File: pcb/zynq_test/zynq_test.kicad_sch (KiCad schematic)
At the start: 0 parts

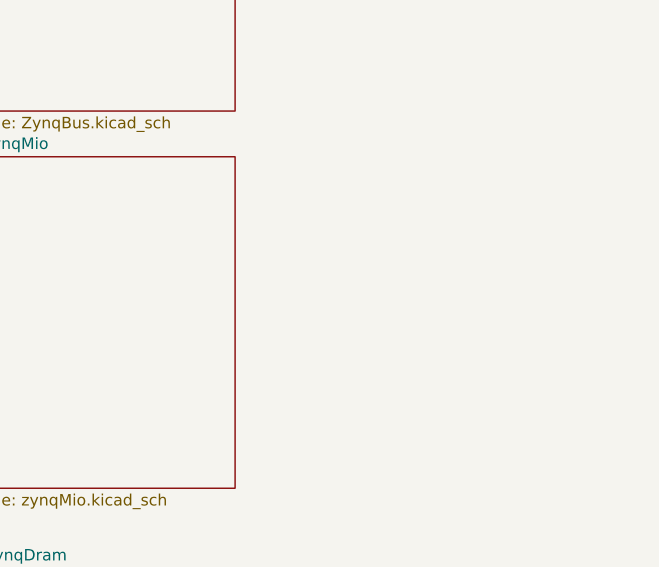
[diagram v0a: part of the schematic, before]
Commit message: Changed MIO signals to Buses
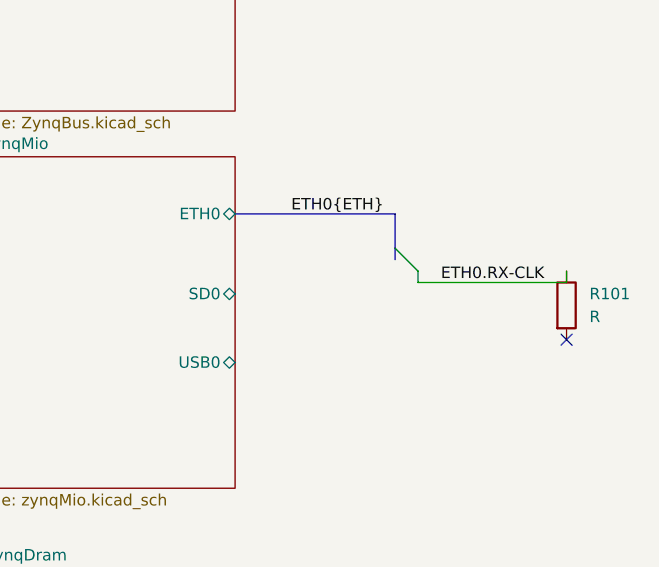
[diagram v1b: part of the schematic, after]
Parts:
- added R101: R, Capacitor_SMD:C_0805_2012Metric, symbol Device:R
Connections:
- new net ETH0.RX-CLK: R101.1
- no-connect marks 0 -> 1
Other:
- sheet zynqMio ports: added ETH0, SD0, USB0; removed none
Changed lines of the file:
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@@
 	(generator_version "9.0")
 	(paper "A4")
+	(no_connect
+		(at 170.18 83.82)
+	)
+	(bus_entry
+		(at 151.13 73.66)
+		(size 2.54 2.54)
+		(stroke
+			(width 0)
+			(type default)
+		)
+	)
+	(bus
+		(pts
+			(xy 151.13 69.85) (xy 151.13 73.66)
+		)
+		(stroke
+			(width 0)
+			(type default)
+		)
+	)
+	(wire
+		(pts
+			(xy 153.67 77.47) (xy 170.18 77.47)
+		)
+		(stroke
+			(width 0)
+			(type default)
+		)
+	)
+	(wire
+		(pts
+			(xy 170.18 77.47) (xy 170.18 76.2)
+		)
+		(stroke
+			(width 0)
+			(type default)
+		)
+	)
+	(wire
+		(pts
+			(xy 153.67 76.2) (xy 153.67 77.47)
+		)
+		(stroke
+			(width 0)
+			(type default)
+		)
+	)
+	(bus
+		(pts
+			(xy 133.35 69.85) (xy 151.13 69.85)
+		)
+		(stroke
+			(width 0)
+			(type default)
+		)
+	)
+	(bus
+		(pts
+			(xy 151.13 73.66) (xy 151.13 74.93)
+		)
+		(stroke
+			(width 0)
+			(type default)
+		)
+	)
+	(label "ETH0{ETH}"
+		(at 149.86 69.85 180)
+		(effects
+			(font
+				(size 1.27 1.27)
+			)
+			(justify right bottom)
+		)
+	)
+	(label "ETH0.RX-CLK"
+		(at 156.21 77.47 0)
+		(effects
+			(font
+				(size 1.27 1.27)
+			)
+			(justify left bottom)
+		)
+	)
+	(symbol
+		(lib_id "Device:R")
+		(at 170.18 80.01 0)
+		(unit 1)
+		(exclude_from_sim no)
+		(in_bom yes)
+		(on_board yes)
+		(dnp no)
+		(fields_autoplaced yes)
+		(property "Reference" "R101"
+			(at 172.72 78.7399 0)
+			(effects
+				(font
+					(size 1.27 1.27)
+				)
+				(justify left)
+			)
+		)
+		(property "Value" "R"
+			(at 172.72 81.2799 0)
+			(effects
+				(font
+					(size 1.27 1.27)
+				)
+				(justify left)
+			)
+		)
+		(property "Footprint" "Capacitor_SMD:C_0805_2012Metric"
+			(at 168.402 80.01 90)
+			(effects
+				(font
+					(size 1.27 1.27)
+				)
+				(hide yes)
+			)
+		)
+		(property "Datasheet" "~"
+			(at 170.18 80.01 0)
+			(effects
+				(font
+					(size 1.27 1.27)
+				)
+				(hide yes)
+			)
+		)
+		(property "Description" "Resistor"
+			(at 170.18 80.01 0)
+			(effects
+				(font
+					(size 1.27 1.27)
+				)
+				(hide yes)
+			)
+		)
+		(pin "1"
+		)
+		(pin "2"
+		)
+		(instances
+			(project ""
+				(path "/0637578d-4ce5-4d31-b973-2de977269ea5"
+					(reference "R101")
+					(unit 1)
+				)
+			)
+		)
+	)
 	(sheet
 		(at 105.41 148.59)
@@
 			)
 		)
+		(pin "ETH0" bidirectional
+			(at 133.35 69.85 0)
+			(effects
+				(font
+					(size 1.27 1.27)
+				)
+				(justify right)
+			)
+		)
+		(pin "SD0" bidirectional
+			(at 133.35 78.74 0)
+			(effects
+				(font
+					(size 1.27 1.27)
+				)
+				(justify right)
+			)
+		)
+		(pin "USB0" bidirectional
+			(at 133.35 86.36 0)
+			(effects
+				(font
+					(size 1.27 1.27)
+				)
+				(justify right)
+			)
+		)

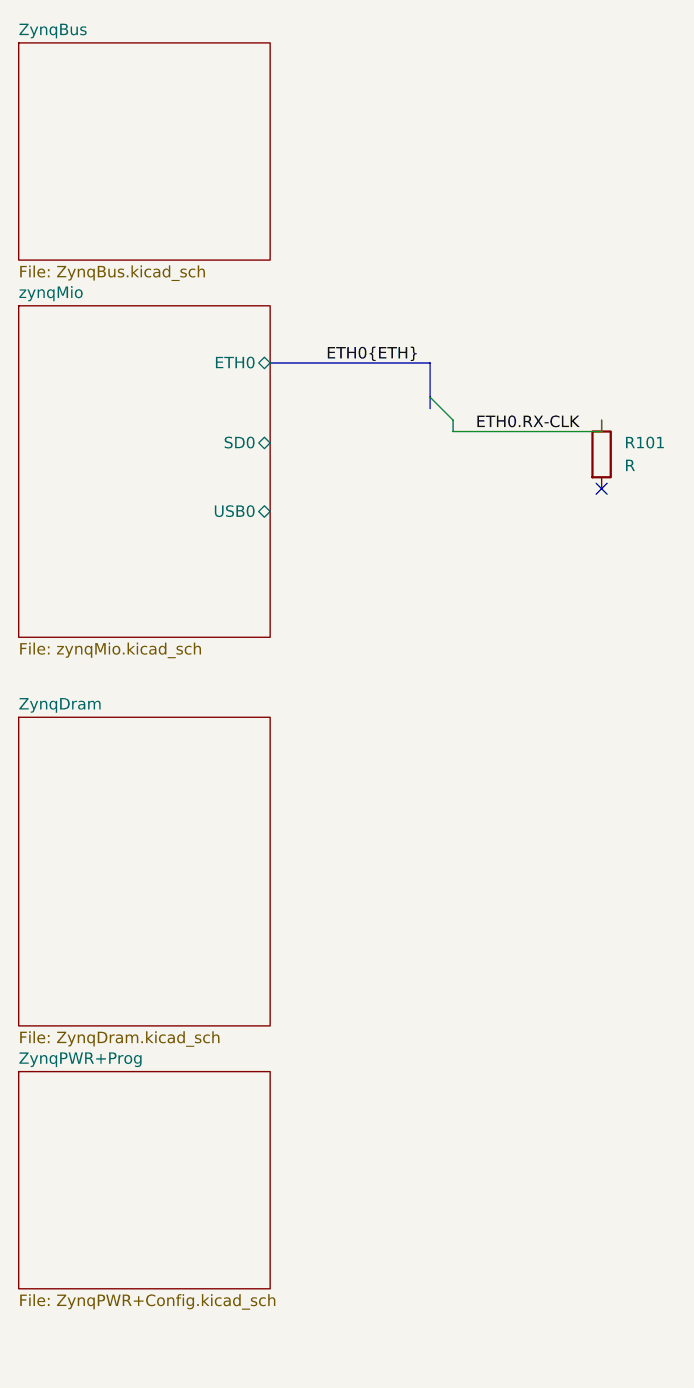
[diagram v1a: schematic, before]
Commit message: Finished PS, started on PWR
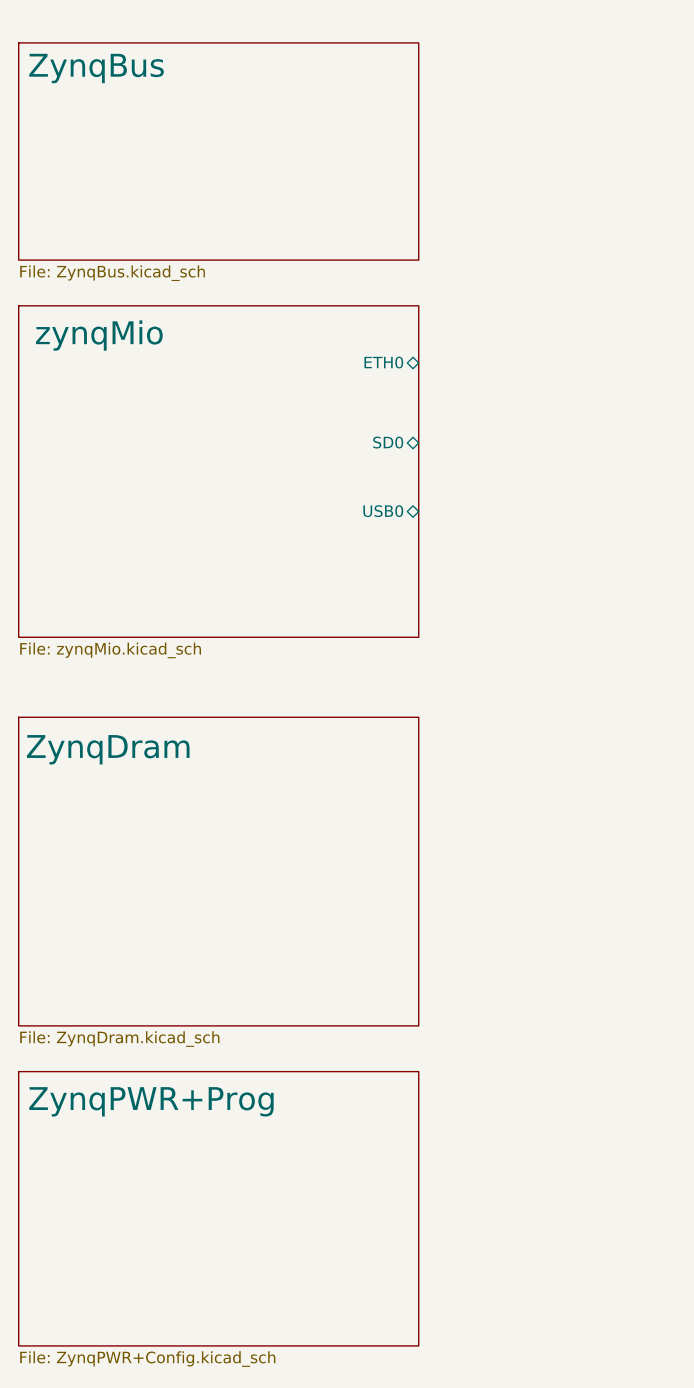
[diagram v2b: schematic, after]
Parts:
- removed R101: R, Capacitor_SMD:C_0805_2012Metric, symbol Device:R
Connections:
- no-connect marks 1 -> 0
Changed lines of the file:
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@@
 	(generator_version "9.0")
 	(paper "A4")
-	(no_connect
-		(at 170.18 83.82)
-	)
-	(bus_entry
-		(at 151.13 73.66)
-		(size 2.54 2.54)
-		(stroke
-			(width 0)
-			(type default)
-		)
-	)
-	(bus
-		(pts
-			(xy 151.13 69.85) (xy 151.13 73.66)
-		)
-		(stroke
-			(width 0)
-			(type default)
-		)
-	)
-	(wire
-		(pts
-			(xy 153.67 77.47) (xy 170.18 77.47)
-		)
-		(stroke
-			(width 0)
-			(type default)
-		)
-	)
-	(wire
-		(pts
-			(xy 170.18 77.47) (xy 170.18 76.2)
-		)
-		(stroke
-			(width 0)
-			(type default)
-		)
-	)
-	(wire
-		(pts
-			(xy 153.67 76.2) (xy 153.67 77.47)
-		)
-		(stroke
-			(width 0)
-			(type default)
-		)
-	)
-	(bus
-		(pts
-			(xy 133.35 69.85) (xy 151.13 69.85)
-		)
-		(stroke
-			(width 0)
-			(type default)
-		)
-	)
-	(bus
-		(pts
-			(xy 151.13 73.66) (xy 151.13 74.93)
-		)
-		(stroke
-			(width 0)
-			(type default)
-		)
-	)
-	(label "ETH0{ETH}"
-		(at 149.86 69.85 180)
-		(effects
-			(font
-				(size 1.27 1.27)
-			)
-			(justify right bottom)
-		)
-	)
-	(label "ETH0.RX-CLK"
-		(at 156.21 77.47 0)
-		(effects
-			(font
-				(size 1.27 1.27)
-			)
-			(justify left bottom)
-		)
-	)
-	(symbol
-		(lib_id "Device:R")
-		(at 170.18 80.01 0)
-		(unit 1)
+	(sheet
+		(at 105.41 148.59)
+		(size 44.45 30.48)
 		(exclude_from_sim no)
 		(in_bom yes)
 		(on_board yes)
 		(dnp no)
-		(fields_autoplaced yes)
-		(property "Reference" "R101"
-			(at 172.72 78.7399 0)
-			(effects
-				(font
-					(size 1.27 1.27)
-				)
-				(justify left)
-			)
-		)
-		(property "Value" "R"
-			(at 172.72 81.2799 0)
-			(effects
-				(font
-					(size 1.27 1.27)
-				)
-				(justify left)
-			)
-		)
-		(property "Footprint" "Capacitor_SMD:C_0805_2012Metric"
-			(at 168.402 80.01 90)
-			(effects
-				(font
-					(size 1.27 1.27)
-				)
-				(hide yes)
-			)
-		)
-		(property "Datasheet" "~"
-			(at 170.18 80.01 0)
-			(effects
-				(font
-					(size 1.27 1.27)
-				)
-				(hide yes)
-			)
-		)
-		(property "Description" "Resistor"
-			(at 170.18 80.01 0)
-			(effects
-				(font
-					(size 1.27 1.27)
-				)
-				(hide yes)
-			)
-		)
-		(pin "1"
-		)
-		(pin "2"
-		)
-		(instances
-			(project ""
-				(path "/0637578d-4ce5-4d31-b973-2de977269ea5"
-					(reference "R101")
-					(unit 1)
-				)
-			)
-		)
-	)
-	(sheet
-		(at 105.41 148.59)
-		(size 27.94 24.13)
-		(exclude_from_sim no)
-		(in_bom yes)
-		(on_board yes)
-		(dnp no)
-		(fields_autoplaced yes)
 		(stroke
 			(width 0.1524)
@@
 		)
 		(property "Sheetname" "ZynqPWR+Prog"
-			(at 105.41 147.8784 0)
+			(at 106.426 153.162 0)
 			(effects
 				(font
-					(size 1.27 1.27)
+					(size 2.54 2.54)
 				)
 				(justify left bottom)
@@
 		)
 		(property "Sheetfile" "ZynqPWR+Config.kicad_sch"
-			(at 105.41 173.3046 0)
+			(at 105.41 179.6546 0)
 			(effects
 				(font
@@
 	(sheet
 		(at 105.41 109.22)
-		(size 27.94 34.29)
+		(size 44.45 34.29)
 		(exclude_from_sim no)
 		(in_bom yes)
 		(on_board yes)
 		(dnp no)
-		(fields_autoplaced yes)
 		(stroke
 			(width 0.1524)
@@
 		)
 		(property "Sheetname" "ZynqDram"
-			(at 105.41 108.5084 0)
+			(at 106.172 114.046 0)
 			(effects
 				(font
-					(size 1.27 1.27)
+					(size 2.54 2.54)
 				)
 				(justify left bottom)
@@
 	(sheet
 		(at 105.41 34.29)
-		(size 27.94 24.13)
+		(size 44.45 24.13)
 		(exclude_from_sim no)
 		(in_bom yes)
 		(on_board yes)
 		(dnp no)
-		(fields_autoplaced yes)
 		(stroke
 			(width 0.1524)
@@
 		)
 		(property "Sheetname" "ZynqBus"
-			(at 105.41 33.5784 0)
+			(at 106.426 38.354 0)
 			(effects
 				(font
-					(size 1.27 1.27)
+					(size 2.54 2.54)
 				)
 				(justify left bottom)
@@
 	(sheet
 		(at 105.41 63.5)
-		(size 27.94 36.83)
+		(size 44.45 36.83)
 		(exclude_from_sim no)
 		(in_bom yes)
 		(on_board yes)
 		(dnp no)
-		(fields_autoplaced yes)
 		(stroke
 			(width 0.1524)
@@
 		)
 		(property "Sheetname" "zynqMio"
-			(at 105.41 62.7884 0)
+			(at 107.188 68.072 0)
 			(effects
 				(font
-					(size 1.27 1.27)
+					(size 2.54 2.54)
 				)
 				(justify left bottom)
@@
 		)
 		(pin "ETH0" bidirectional
-			(at 133.35 69.85 0)
+			(at 149.86 69.85 0)
 			(effects
 				(font
@@
 		)
 		(pin "SD0" bidirectional
-			(at 133.35 78.74 0)
+			(at 149.86 78.74 0)
 			(effects
 				(font
@@
 		)
 		(pin "USB0" bidirectional
-			(at 133.35 86.36 0)
+			(at 149.86 86.36 0)
 			(effects
 				(font
